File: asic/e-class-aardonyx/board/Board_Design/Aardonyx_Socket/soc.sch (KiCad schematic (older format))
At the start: 111 parts, among them SW3 SW_DIP_x03, U15 SKT32E

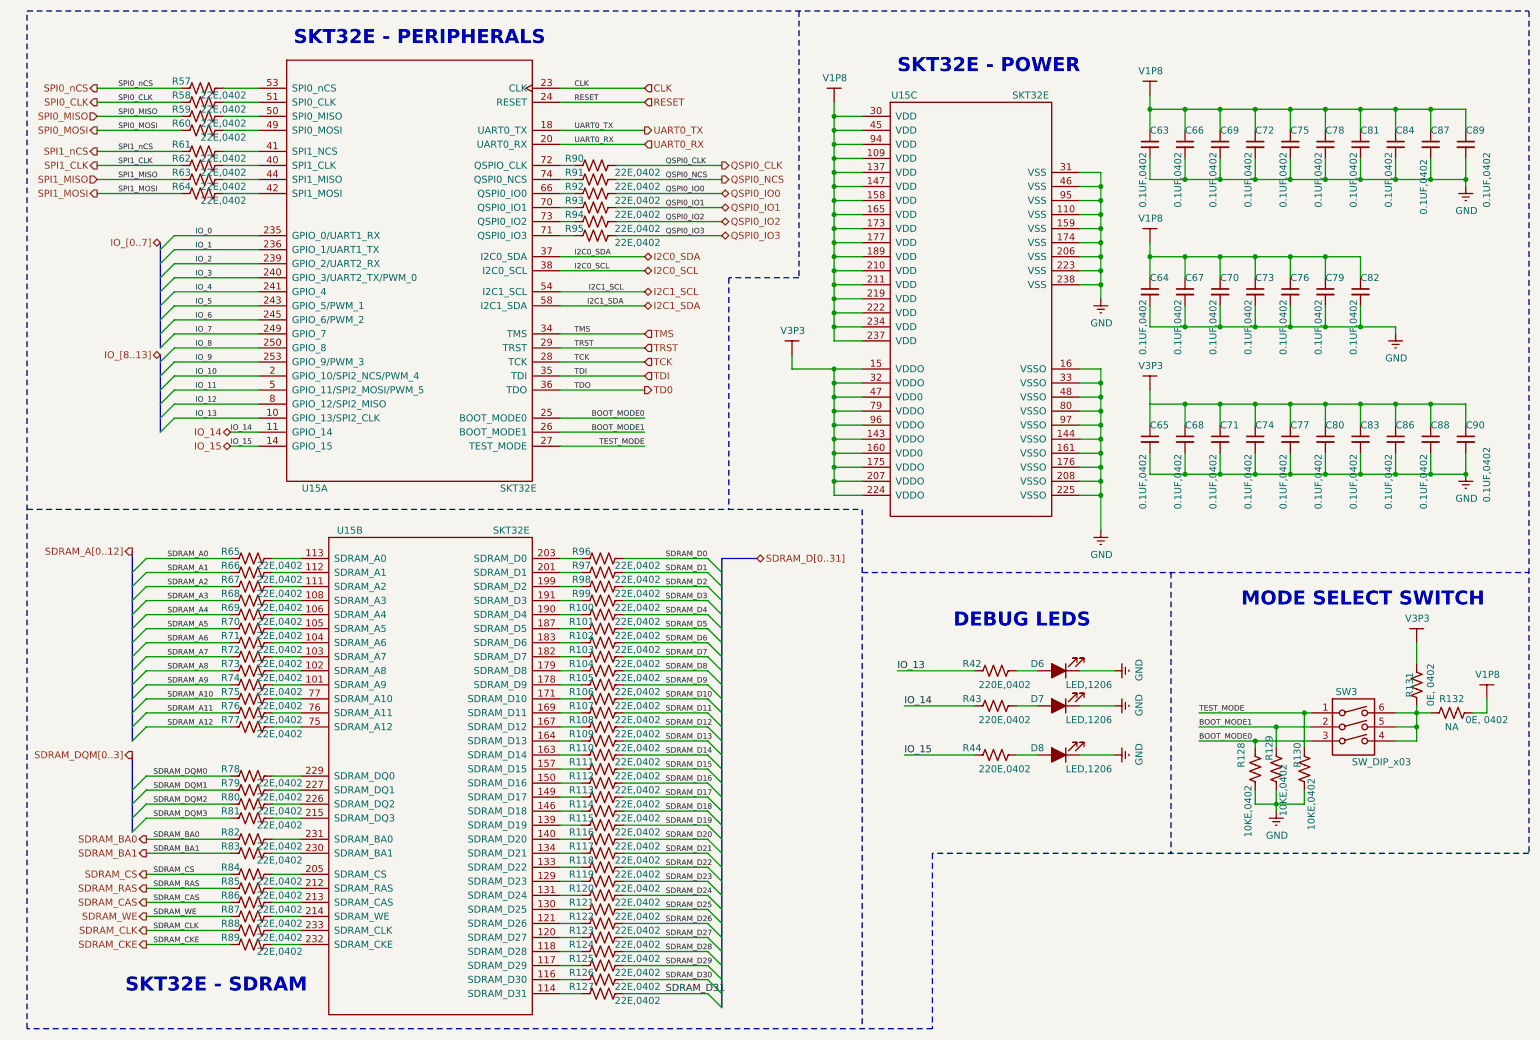
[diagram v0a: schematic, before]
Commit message: update socket compo placement
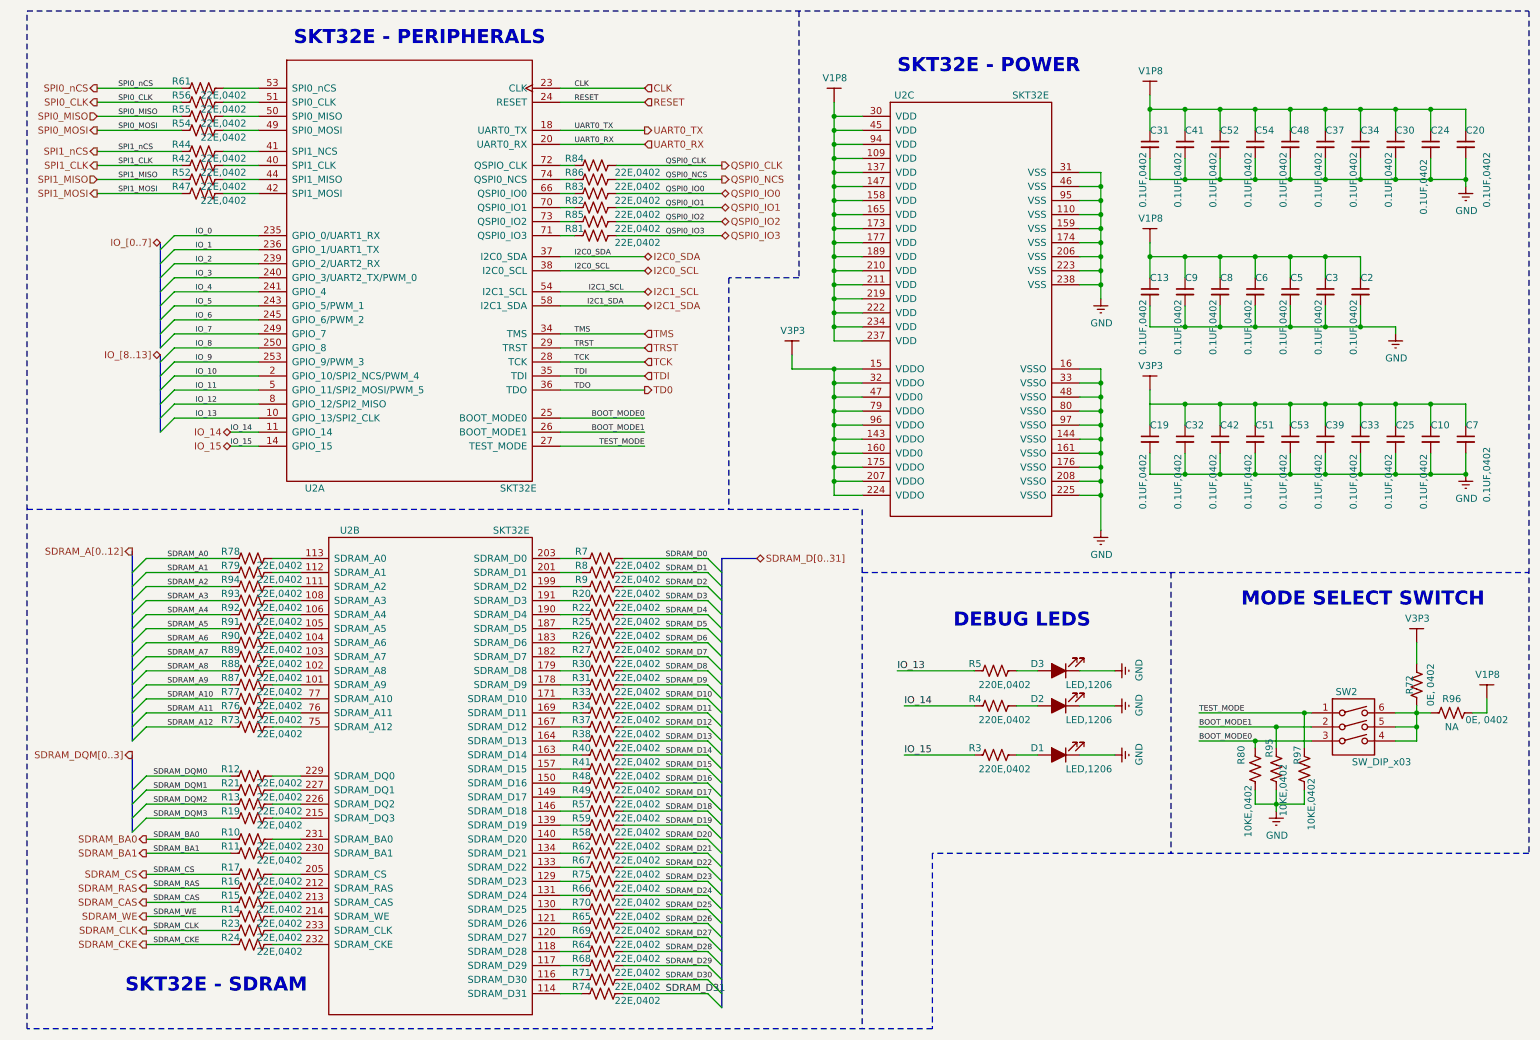
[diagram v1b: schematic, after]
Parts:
- renumbered C88 to C10, C64 to C13, C65 to C19, C82 to C2, C89 to C20, C87 to C24, C86 to C25, C79 to C3, C84 to C30, C63 to C31, C68 to C32, C83 to C33, C81 to C34, C78 to C37, C80 to C39, C66 to C41, C71 to C42, C75 to C48, C76 to C5, C74 to C51, C69 to C52, C77 to C53, C72 to C54, C73 to C6, C90 to C7, C70 to C8, C67 to C9, D8 to D1, D7 to D2, D6 to D3, R82 to R10, R83 to R11, R78 to R12, R80 to R13, R87 to R14, R86 to R15, R85 to R16, R84 to R17, R81 to R19, R99 to R20, R79 to R21, R100 to R22, R88 to R23, R89 to R24, R101 to R25, R102 to R26, R103 to R27, R44 to R3, R104 to R30, R105 to R31, R106 to R33, R107 to R34, R108 to R37, R109 to R38, R43 to R4, R110 to R40, R111 to R41, R62 to R42, R61 to R44, R64 to R47, R112 to R48, R113 to R49, R42 to R5, R63 to R52, R60 to R54, R59 to R55, R58 to R56, R114 to R57, R116 to R58, R115 to R59, R57 to R61, R117 to R62, R124 to R64, R122 to R65, R120 to R66, R118 to R67, R125 to R68, R123 to R69, R96 to R7, R121 to R70, R126 to R71, R131 to R72, R77 to R73, R127 to R74, R119 to R75, R75 to R77, R65 to R78, R66 to R79, R97 to R8, R128 to R80, R95 to R81, R93 to R82, R92 to R83, R90 to R84, R94 to R85, R91 to R86, R74 to R87, R73 to R88, R72 to R89, R98 to R9, R71 to R90, R70 to R91, R69 to R92, R68 to R93, R67 to R94, R129 to R95, R132 to R96, R130 to R97, SW3 to SW2, U15 to U2

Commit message: Back annotation
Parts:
- renumbered C3 to C10, C5 to C12, C6 to C13, C8 to C14, C9 to C15, C13 to C16, C25 to C21, C24 to C22, C31 to C24, C30 to C25, C32 to C27, C34 to C28, C33 to C31, C41 to C33, C37 to C34, C42 to C37, C7 to C4, C39 to C40, C48 to C41, C54 to C46, C52 to C49, C51 to C53, C53 to C54, C10 to C6, C2 to C9, R3 to R1, R79 to R100, R78 to R101, R81 to R115, R82 to R116, R85 to R117, R84 to R118, R83 to R119, R23 to R12, R86 to R120, R12 to R13, R24 to R14, R21 to R15, R14 to R16, R15 to R17, R16 to R18, R17 to R19, R4 to R2, R7 to R20, R72 to R21, R8 to R22, R9 to R23, R80 to R24, R95 to R26, R96 to R27, R97 to R28, R19 to R29, R5 to R3, R10 to R30, R11 to R31, R20 to R32, R13 to R33, R22 to R34, R25 to R35, R26 to R36, R27 to R37, R30 to R38, R31 to R40, R33 to R41, R34 to R42, R37 to R43, R38 to R44, R40 to R47, R41 to R48, R48 to R51, R42 to R53, R49 to R54, R44 to R55, R57 to R56, R47 to R58, R52 to R59, R59 to R60, R58 to R61, R54 to R62, R55 to R63, R61 to R64, R56 to R65, R62 to R66, R75 to R70, R74 to R71, R71 to R72, R68 to R73, R64 to R74, R70 to R75, R66 to R76, R65 to R87, R69 to R88, R77 to R89, R73 to R90, R76 to R91, R87 to R92, R88 to R93, R89 to R94, R90 to R95, R91 to R96, R92 to R97, R93 to R98, R94 to R99, U2 to U1
